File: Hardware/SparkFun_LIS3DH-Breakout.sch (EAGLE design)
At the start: 16 parts, among them U1 MMA8452Q

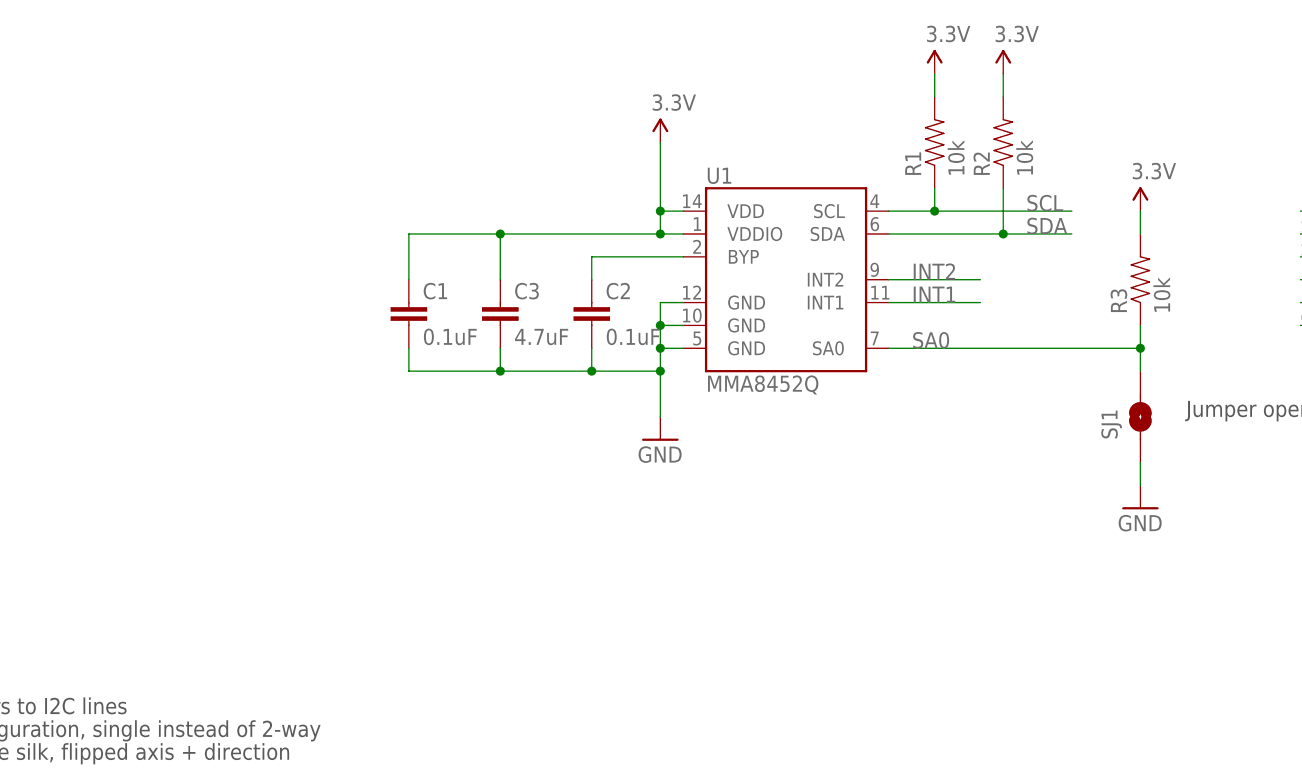
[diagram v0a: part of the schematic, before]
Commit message: Implanted LIS3DH into previous design, renamed files but basically the design is still really the old design with the new IC.  This is a turning point before adding more features.  Also, the gitignore file has been updated to include eagle backups and locks.
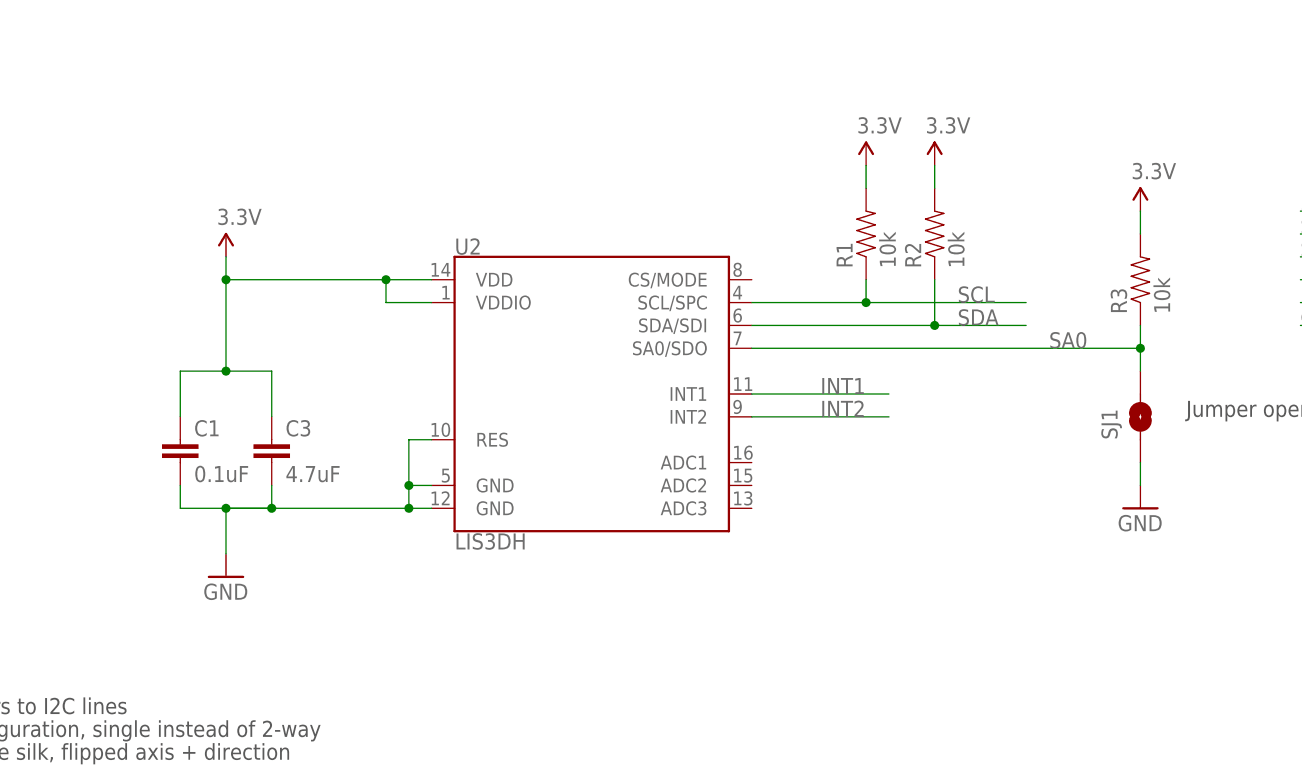
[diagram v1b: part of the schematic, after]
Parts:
- removed C2: 0.1uF, SparkFun:CAP0402-CAP
- removed U1: MMA8452Q, SparkFun:MMA8452Q
- added U2: LIS3DH, SparkFun-Sensors:LIS3DH
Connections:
- removed net BYP: C2.1, U1.BYP
- net 3.3V: now also U2.VDD, U2.VDDIO; no longer U1.VDD, U1.VDDIO
- net GND: now also U2.GND@12, U2.GND@5, U2.RES; no longer C2.2, U1.GND@0, U1.GND@1, U1.GND@2
- net INT1: now also U2.INT1; no longer U1.INT1
- net INT2: now also U2.INT2; no longer U1.INT2
- net SA0: now also U2.SA0/SDO; no longer U1.SA0
- net SCL: now also U2.SCL/SPC; no longer U1.SCL
- net SDA: now also U2.SDA/SDI; no longer U1.SDA
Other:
- moved on the sheet: C1, C3, R1, R2

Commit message: Finished design for proto 1
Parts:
- removed JP1: LOGO-SFESK, SparkFun:LOGO-SFESK
- removed JP5: (no value), SparkFun:M06SIP
- removed U$2: CREATIVE_COMMONS, SparkFun:CREATIVE_COMMONS
- added FRAME2: FRAME-LETTER, SparkFun-Aesthetics:FRAME-LETTER
- added J1: (no value), SparkFun-Connectors:CONN_06SILK_FEMALE_PTH
- added J2: (no value), SparkFun-Connectors:CONN_05PTH
- added LOGO1: SFE_LOGO_FLAME.1_INCH, SparkFun-Aesthetics:SFE_LOGO_FLAME.1_INCH
- added R4: 10k, SparkFun-Resistors:10KOHM-0603-1/10W-1%
- added SJ2: (no value), TestAperatures:JUMPER-PAD-3-NC_BY_TRACE
- R1, R2: value 10k -> 4.7k; device SparkFun:RESISTOR0402-RES -> SparkFun-Resistors:4.7KOHM-0603-1/10W-1%
- R3: device SparkFun:RESISTOR0402-RES -> SparkFun-Resistors:10KOHM-0603-1/10W-1%
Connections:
- new net ADC1: J2.1, U2.ADC1
- new net ADC2: J2.2, U2.ADC2
- new net ADC3: J2.3, U2.ADC3
- new net CS: J1.6, R4.1, U2.CS/MODE
- new net N$1: R2.2, SJ2.1
- new net N$2: R1.2, SJ2.3
- net 3.3V: now also J1.2, R4.2, SJ2.2; no longer JP5.1, R1.2, R2.2
- net GND: now also J1.1; no longer JP5.6
- net INT1: now also J2.5; no longer JP5.5
- net INT2: now also J2.4; no longer JP5.4
- net SA0: now also J1.5
- net SCL: now also J1.4; no longer JP5.3
- net SDA: now also J1.3; no longer JP5.2
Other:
- note added: "Accelerometer Circuitry"
- note added: "Apply 1.8v to 3.3v between "3.3V" and "GND""
- note added: "LIS3DH Breakout"
- note added: "MODES: I2C: Leave the copper-connected jumper SJ2 as default, use SJ1 to set the I2C address between 0x18 and 0x19. SJ1 is the LSB of the address. SPI 4-WIRE: Jumpers SJ2 can be opened to remove 4.7k load on the SPI lines. Open SJ1"
- note added: "Marshall Taylor"
- note added: "SA0 = 0: 0x18"
- note added: "SA0 = 1: 0x19"
- note added: "SJ2 pulls up the SCK and SDA lines for I2C operation"
- note added: "User Ports"
- note added: "v01"
- note removed: "* Added 10k pull-up resistors to I2C lines"
- note removed: "* Changed the jumper configuration, single instead of 2-way"
- note removed: "* Minor adjustments to some silk, flipped axis + direction"
- note removed: "Jim Lindblom"
- note removed: "SA0 = 0: 0x1C"
- note removed: "SA0 = 1: 0x1D"
- note removed: "v11"
- note removed: "v11 Changelog"
- moved on the sheet: C1, C3, R1, R2, R3, SJ1, U2

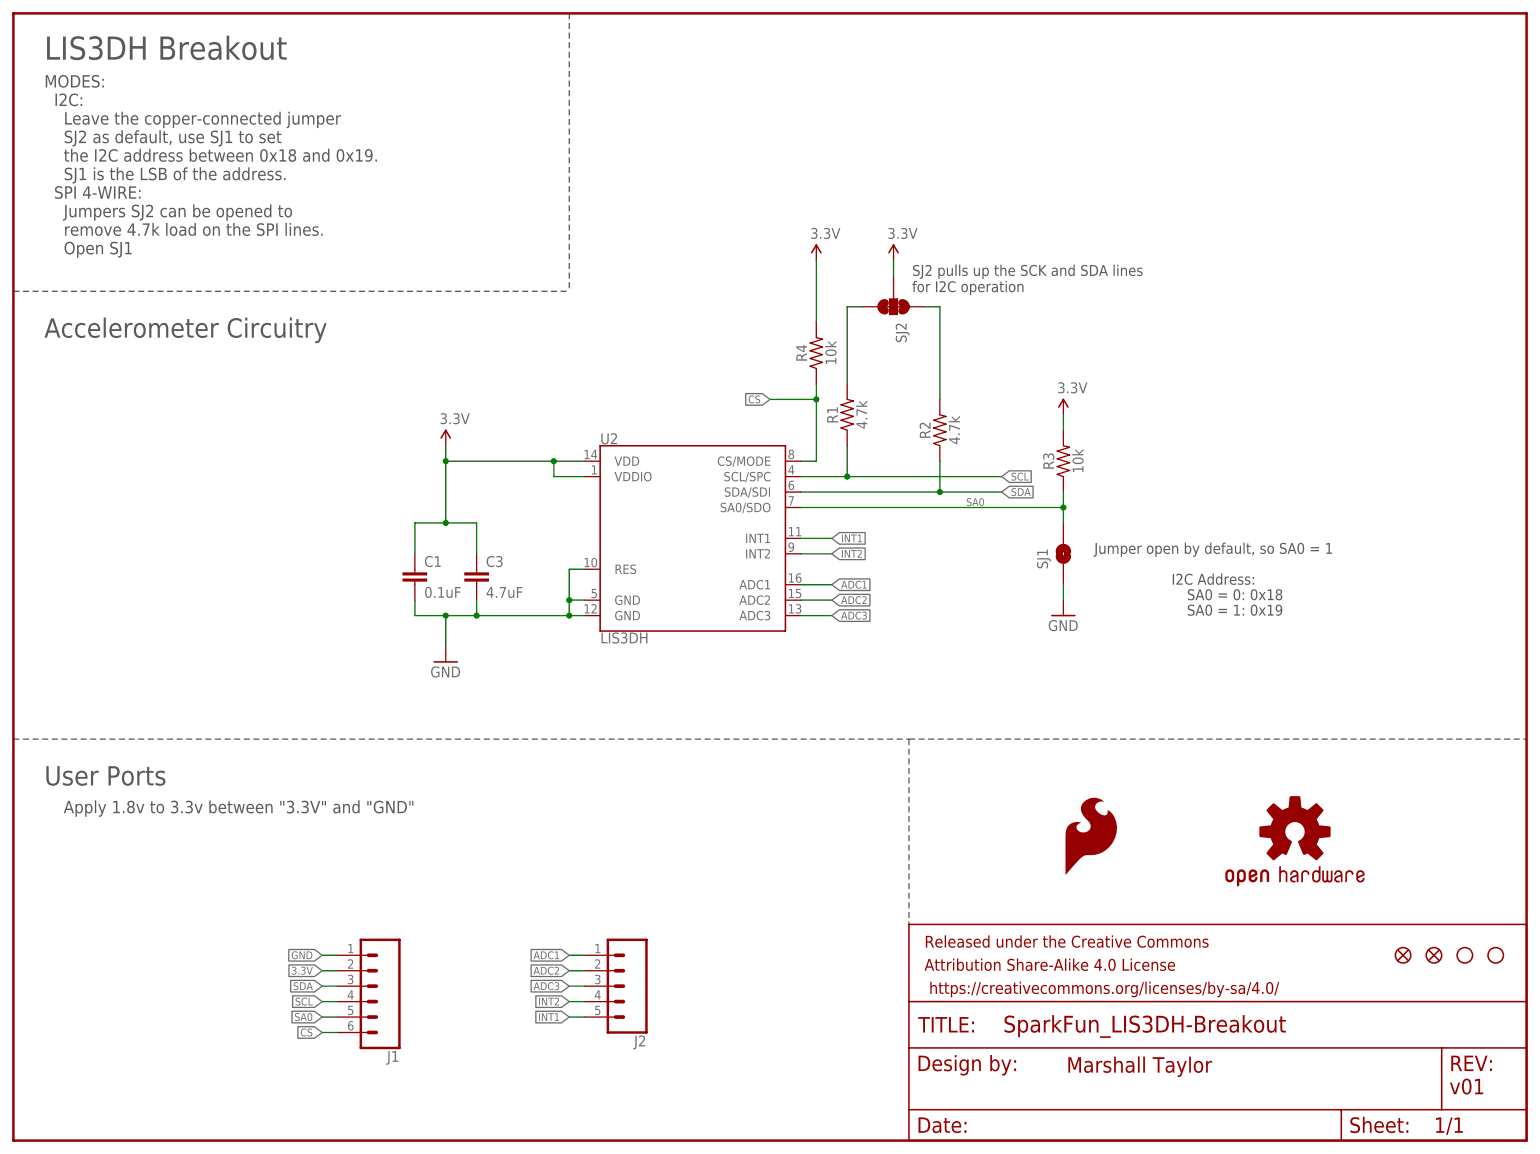
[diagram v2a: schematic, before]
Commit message: Updated design based off design review
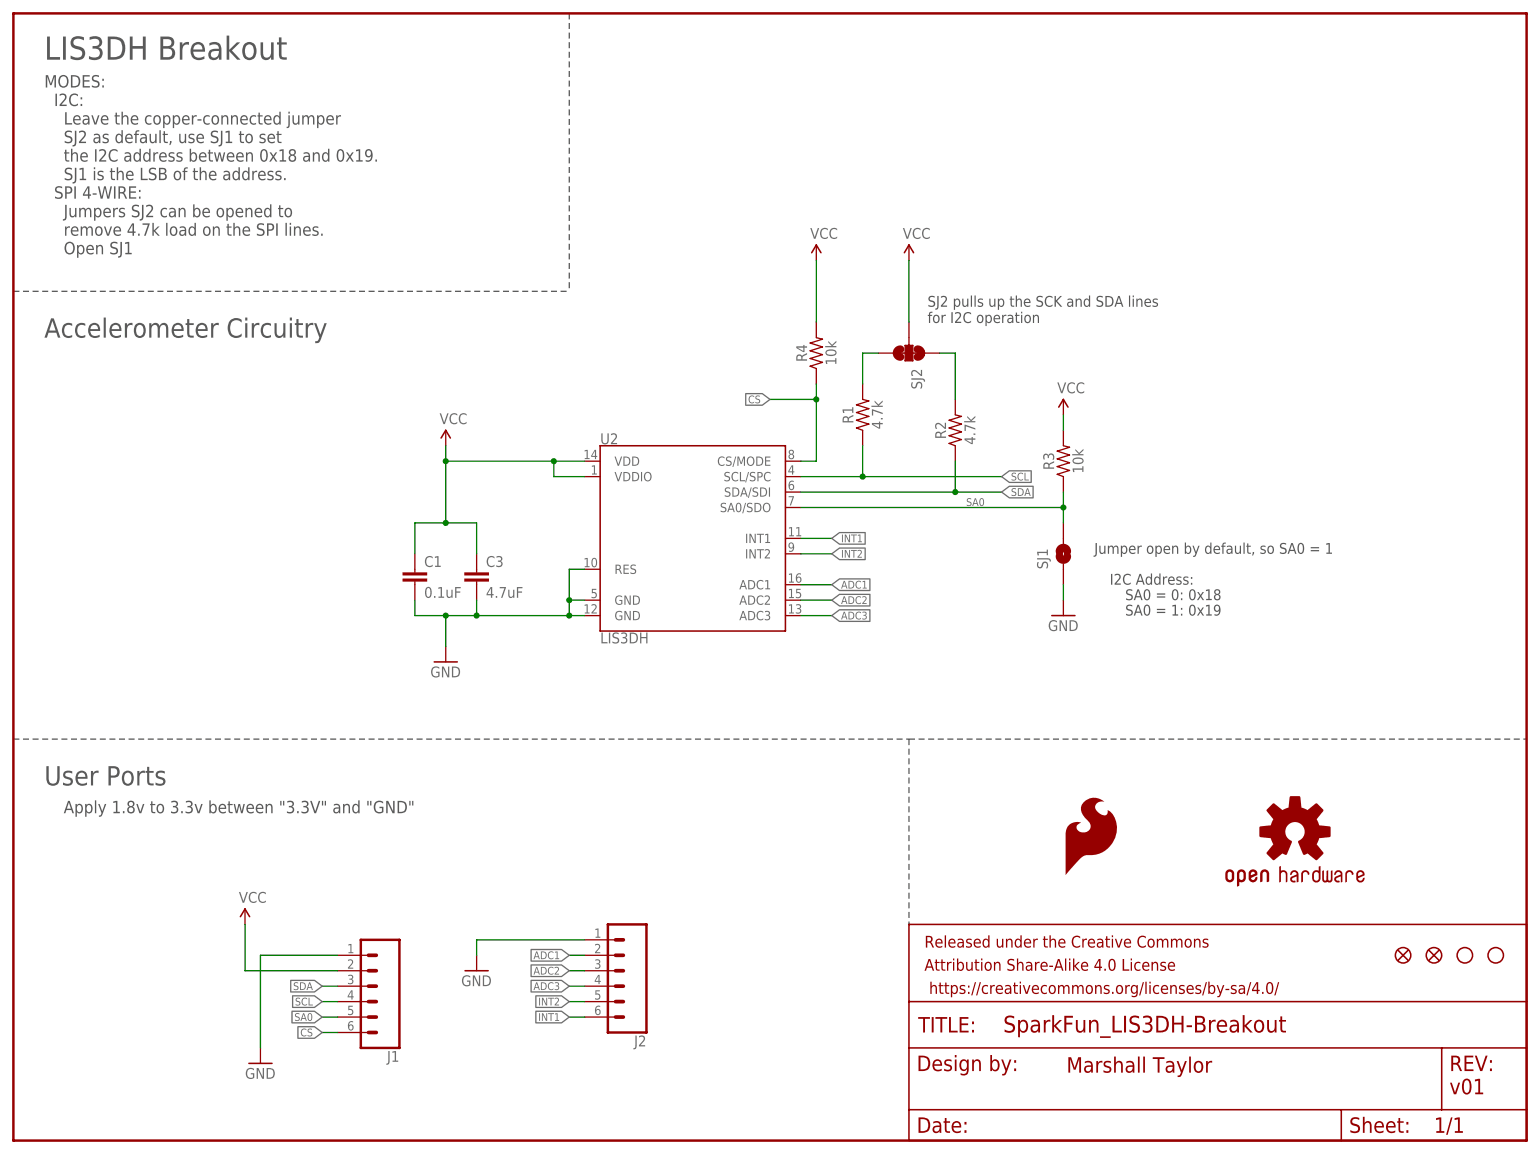
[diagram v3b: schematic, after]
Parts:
- J2: device SparkFun-Connectors:CONN_05PTH -> SparkFun-Connectors:CONN_06SILK_FEMALE_PTH
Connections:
- new net VCC: J1.2
- net 3.3V: no longer J1.2
- net ADC1: now also J2.2; no longer J2.1
- net ADC2: now also J2.3; no longer J2.2
- net ADC3: now also J2.4; no longer J2.3
- net GND: now also J2.1
- net INT1: now also J2.6; no longer J2.5
- net INT2: now also J2.5; no longer J2.4
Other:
- moved on the sheet: R1, R2, SJ2
